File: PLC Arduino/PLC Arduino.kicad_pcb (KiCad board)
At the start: 2 copper layers, 145 x 75 mm, 208 parts, among them J1 Screw_Terminal_01x12, J2 Screw_Terminal_01x12, J3 Screw_Terminal_01x12, J4 Screw_Terminal_01x12, J5 USB_B_Micro, J6 Conn_01x04_Socket, J7 Conn_01x03_Socket, J8 Conn_01x02_Socket, J9 Conn_01x02_Socket, K1 SANYOU_SRD_Form_C, K2 SANYOU_SRD_Form_C, K3 SANYOU_SRD_Form_C, K5 SANYOU_SRD_Form_C, Q1 Q_NMOS_Depletion_GSD, Q10 BSS138, Q2 Q_NMOS_Depletion_GSD, Q3 Q_NMOS_Depletion_GSD, Q4 Q_NMOS_Depletion_GSD, Q5 Q_NMOS_Depletion_GSD, Q6 Q_NMOS_Depletion_GSD, Q7 Q_NMOS_Depletion_GSD, Q8 Q_NMOS_Depletion_GSD, Q9 BSS138, SW1 SW_Push, SW2 SW_Push, U1 PC817, U10 PC817, U11 PC817, U12 PC817, U13 PC817, U14 PC817, U15 PC817, U16 PC817, U18 ADS1115IDGS, U2 PC817, U22 ISO1540, U23 ESP32-WROOM-32, U24 CH340C, U25 MAX485E, U26 MAX485E, U27 TPL5010, U28 B0505S-2WR3, U29 LM2596S-5, U3 PC817, U30 AMS1117-3.3, U31 AMS1117-3.3, U32 74HC595, U33 74HC595, U34 74HC4051, U4 PC817, U5 PC817, U6 PC817, U7 PC817, U8 PC817, U9 PC817

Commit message: Done Layout PCB
To Do Zoning
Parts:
- removed C24: 220uF, Capacitor_SMD:C_Elec_6.3x7.7
- added C5: 100uF, Capacitor_SMD:C_1210_3225Metric_Pad1.33x2.70mm_HandSolder, F.Cu at (42.5, 26.6)
- added C6: 100uF, Capacitor_SMD:C_1210_3225Metric_Pad1.33x2.70mm_HandSolder, F.Cu at (46.0, 26.6)
- added J10: Conn_01x03_Socket, Connector_PinHeader_2.54mm:PinHeader_1x03_P2.54mm_Vertical, F.Cu at (145.3, 21.9)
- added J11: Conn_01x05_Socket, Connector_PinHeader_2.54mm:PinHeader_1x05_P2.54mm_Vertical, F.Cu at (145.3, 32.7)
- added J12: Conn_01x03_Socket, Connector_PinHeader_2.54mm:PinHeader_1x03_P2.54mm_Vertical, F.Cu at (136.5, 49.9)
- added J13: Conn_01x05_Socket, Connector_PinHeader_2.54mm:PinHeader_1x05_P2.54mm_Vertical, F.Cu at (63.9, 64.5)
- added J14: Screw_Terminal_01x08, TerminalBlock:TerminalBlock_bornier-8_P5.08mm, F.Cu at (183.8, 19.8)
- added J15: Screw_Terminal_01x08, TerminalBlock:TerminalBlock_bornier-8_P5.08mm, F.Cu at (127.8, 68.2)
- added JP19: SolderJumper_3_Open, Jumper:SolderJumper-3_P1.3mm_Open_Pad1.0x1.5mm, F.Cu at (59.3, 45.6)
- added REF**: MountingHole_3.2mm_M3, MountingHole:MountingHole_3.2mm_M3, F.Cu at (127.4, 29.5)
- added REF**: MountingHole_3.2mm_M3, MountingHole:MountingHole_3.2mm_M3, F.Cu at (181.8, 14.2)
- added REF**: MountingHole_3.2mm_M3, MountingHole:MountingHole_3.2mm_M3, F.Cu at (80.9, 29.5)
- added REF**: MountingHole_3.2mm_M3, MountingHole:MountingHole_3.2mm_M3, F.Cu at (86.7, 60.9)
- added REF**: MountingHole_3.2mm_M3, MountingHole:MountingHole_3.2mm_M3, F.Cu at (181.8, 60.7)
- added REF**: MountingHole_3.2mm_M3, MountingHole:MountingHole_3.2mm_M3, F.Cu at (150.4, 20.0)
- C23, C26: footprint Capacitor_SMD:C_Elec_10x10.2 -> Capacitor_SMD:C_1210_3225Metric_Pad1.33x2.70mm_HandSolder
- J4, JP11, JP12, JP13, JP14, JP15, JP16, JP17, JP18: moved to B.Cu
- moved R62 278.1 mm to (30.1, 61.7), turned to 0 degrees
- moved R64 276.7 mm to (30.1, 59.5), turned to 180 degrees
- moved R63 275.3 mm to (30.1, 57.4), turned to 0 degrees
- moved C32 268.5 mm to (63.5, 45.5), turned to 0 degrees
- moved R56 268.0 mm to (48.4, 61.9), turned to 0 degrees
- moved R77 268.0 mm to (61.7, 41.6), turned to -90 degrees
- moved R58 266.3 mm to (48.4, 59.7), turned to 180 degrees
- moved R76 265.7 mm to (63.1, 41.6), turned to -90 degrees
- moved C33 265.2 mm to (64.5, 43.8), turned to 180 degrees
- moved U26 264.6 mm to (36.5, 59.5), turned to 180 degrees
- moved R57 264.5 mm to (48.4, 57.5), turned to 0 degrees
- moved C17 262.3 mm to (52.0, 63.1)
- moved C16 261.9 mm to (53.0, 64.8), turned to 180 degrees
- moved C18 261.2 mm to (34.8, 64.9), turned to 180 degrees
- moved U22 255.8 mm to (67.9, 40.3), turned to 180 degrees
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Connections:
- C1 pad 1: +5VA -> 5VOUT
- C2 pad 2: +5VA -> 5VOUT
- C21 pad 2: +5VA -> 5VOUT
- C23 pad 1: DC_IN_1_B -> 5VOUT
- C23 pad 2: +5VA -> DC_IN_1_B
- C26 pad 1: GNDD -> +5V
- C26 pad 2: +5V -> GNDD
- C27 pad 1: +5VA -> 5VOUT
- C28 pad 2: +5VA -> 5VOUT
- C29 pad 2: +3.3VA -> 3.3VOUT
- C7 pad 2: +5VA -> 5VOUT
- C8 pad 1: +5VA -> 5VOUT
- D10 pad 2: +24V -> 24V_EXT
- D12 pad 2: +24V -> 24V_EXT
- D6 pad 2: +24V -> 24V_EXT
- D7 pad 2: +24V -> 24V_EXT
- J2 pad 5: SLAVE_MODBUS_A -> unconnected-(J2-Pin_5-Pad5)
- J2 pad 6: SLAVE_MODBUS_B -> unconnected-(J2-Pin_6-Pad6)
- J3 pad 1: DC_OUT_1_A -> _DC_OUT_1_A
- J3 pad 2: DC_OUT_1_B -> _DC_OUT_1_B
- J3 pad 3: DC_OUT_2_A -> _DC_OUT_2_A
- J3 pad 4: DC_OUT_2_B -> _DC_OUT_2_B
- J3 pad 5: DC_OUT_3_A -> _DC_OUT_3_A
- J3 pad 6: DC_OUT_3_B -> _DC_OUT_3_B
- J3 pad 7: DC_OUT_4_A -> _DC_OUT_4_A
- J3 pad 8: DC_OUT_4_B -> _DC_OUT_4_B
- J4 pad 10: 5VOUT -> unconnected-(J4-Pin_10-Pad10)
- J4 pad 2: unconnected-(J4-Pin_2-Pad2) -> SLAVE_MODBUS_A
- J4 pad 3: unconnected-(J4-Pin_3-Pad3) -> SLAVE_MODBUS_B
- J4 pad 5: unconnected-(J4-Pin_5-Pad5) -> DC_IN_1_B
- J4 pad 6: DC_IN_1_B -> SCL_E
- J4 pad 7: SCL_E -> SDA_E
- J4 pad 8: SDA_E -> unconnected-(J4-Pin_8-Pad8)
- J4 pad 9: 3.3VOUT -> unconnected-(J4-Pin_9-Pad9)
- J8 pad 2: +5VA -> 5VOUT
- JP10 pad 1: +5VA -> 5VOUT
- JP10 pad 3: +3.3VA -> 3.3VOUT
- JP2 pad 2: +5VA -> 5VOUT
- JP3 pad 1: +5VA -> 5VOUT
- JP3 pad 3: +3.3VA -> 3.3VOUT
- K1 pad 5: +24V -> 24V_EXT
- K2 pad 5: +24V -> 24V_EXT
- K3 pad 5: +24V -> 24V_EXT
- K5 pad 5: +24V -> 24V_EXT
- L1 pad 2: +5VA -> 5VOUT
- Q5 pad 2: DC_IN_1_B -> GND_ANALOG_EXT
- Q6 pad 2: DC_IN_1_B -> GND_ANALOG_EXT
- Q7 pad 2: DC_IN_1_B -> GND_ANALOG_EXT
- Q8 pad 2: DC_IN_1_B -> GND_ANALOG_EXT
- R13 pad 2: DC_IN_1_B -> GND_ANALOG_EXT
- R14 pad 1: DC_DRV_2 -> DC_DRV_2_EXT
- R15 pad 1: +24V -> 24V_EXT
- R16 pad 1: DC_DRV_1 -> DC_DRV_1_EXT
- R17 pad 1: +24V -> 24V_EXT
- R18 pad 2: DC_IN_1_B -> GND_ANALOG_EXT
- R19 pad 1: DC_DRV_3 -> DC_DRV_3_EXT
- R20 pad 1: +24V -> 24V_EXT
- R21 pad 2: DC_IN_1_B -> GND_ANALOG_EXT
- R22 pad 1: DC_DRV_4 -> DC_DRV_4_EXT
- R23 pad 1: +24V -> 24V_EXT
- R24 pad 2: DC_IN_1_B -> GND_ANALOG_EXT
- R67 pad 1: +5VA -> 5VOUT
- R78 pad 2: +5VA -> 5VOUT
- R79 pad 2: +5VA -> 5VOUT
- U18 pad 8: +5VA -> 5VOUT
- U22 pad 1: +5VA -> 5VOUT
- U23 pad 13: SLAVE_RO -> DIG_IN
- U23 pad 16: SLAVE_DI -> WDT_DONE
- U23 pad 30: WDT_DONE -> SLAVE_DI
- U23 pad 31: DIG_IN -> SLAVE_RO
- U28 pad 1: +5VA -> 5VOUT
- U30 pad 2: +3.3VA -> 3.3VOUT
- U30 pad 3: +5VA -> 5VOUT
- U5 pad 1: +3.3V -> 3v3_EXT
- U5 pad 4: VCOUPLER -> VCOUPLER_EXT
- U6 pad 1: +3.3V -> 3v3_EXT
- U6 pad 4: VCOUPLER -> VCOUPLER_EXT
- U7 pad 1: +3.3V -> 3v3_EXT
- U7 pad 4: VCOUPLER -> VCOUPLER_EXT
- U8 pad 1: +3.3V -> 3v3_EXT
- U8 pad 4: VCOUPLER -> VCOUPLER_EXT
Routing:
- net GNDD: track 0.00 -> 487.8 mm, vias 0 -> 33
- net DC_IN_1_B: track 0.00 -> 471.7 mm, vias 0 -> 117
- net +5V: track 0.00 -> 320.3 mm, vias 0 -> 13
- net +3.3V: track 0.00 -> 316.0 mm, vias 0 -> 18
- net +24V: track 0.00 -> 249.7 mm, vias 0 -> 8
- net 5VOUT: track 0.00 -> 232.4 mm, vias 0 -> 7
- net 24V_EXT: track 0.00 -> 139.8 mm, vias 0 -> 4
- net GND_ANALOG_EXT: track 0.00 -> 137.1 mm, vias 0 -> 6
- net DIG_IN: track 0.00 -> 115.3 mm, vias 0 -> 4
- net 3.3VOUT: track 0.00 -> 104.3 mm, vias 0 -> 1
- net VCOUPLER: track 0.00 -> 100.4 mm, vias 0 -> 6
- net SDA_E: track 0.00 -> 97.7 mm, vias 0 -> 4
- net SCL_E: track 0.00 -> 97.1 mm, vias 0 -> 4
- net 3v3_EXT: track 0.00 -> 93.7 mm
- net ESP_SCL: track 0.00 -> 86.4 mm, vias 0 -> 2
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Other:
- board size 145 x 75 mm -> 195.3 x 75 mm

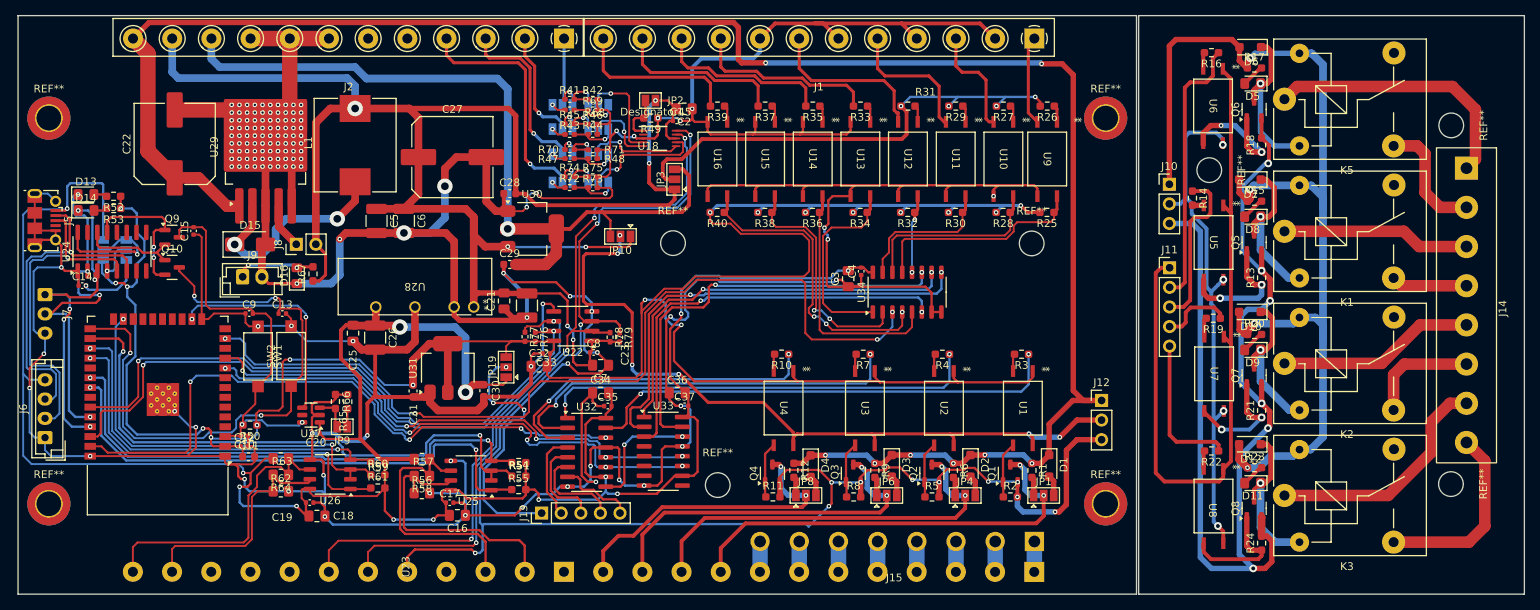
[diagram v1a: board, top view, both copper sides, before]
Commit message: Done PCB Layout PLC Board
To DO:

Review from Nes
Round Corners of Strobe and PLC
Proper Labels PLC Board
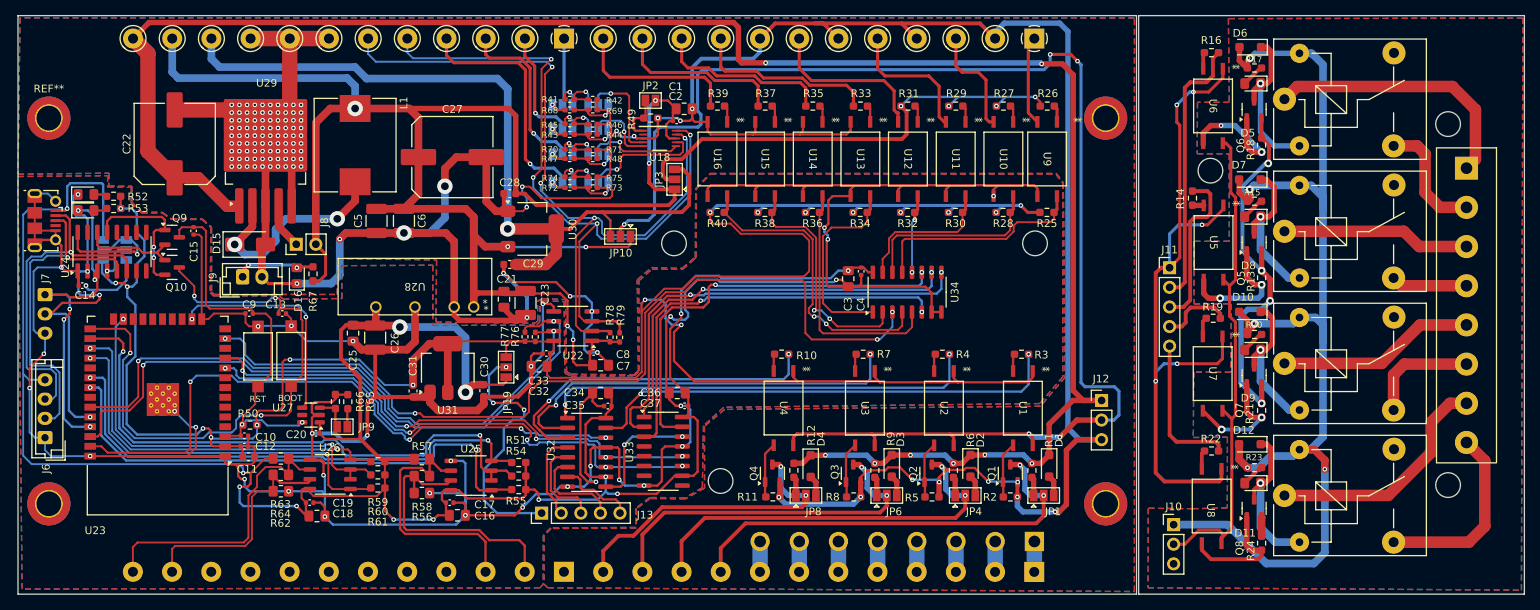
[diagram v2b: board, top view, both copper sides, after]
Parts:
- removed the REF** at (127.4, 29.5)
- removed the REF** at (181.8, 14.2)
- removed the REF** at (80.9, 29.5)
- removed the REF** at (86.7, 60.9)
- removed the REF** at (181.8, 60.7)
- removed the REF** at (150.4, 20.0)
- added REF**: MountingHole_3.2mm_M3, MountingHole:MountingHole_3.2mm_M3, F.Cu at (181.4, 60.9)
- added REF**: MountingHole_3.2mm_M3, MountingHole:MountingHole_3.2mm_M3, F.Cu at (87.1, 60.3)
- added REF**: MountingHole_3.2mm_M3, MountingHole:MountingHole_3.2mm_M3, F.Cu at (150.6, 20.1)
- added REF**: MountingHole_3.2mm_M3, MountingHole:MountingHole_3.2mm_M3, F.Cu at (81.0, 29.5)
- added REF**: MountingHole_3.2mm_M3, MountingHole:MountingHole_3.2mm_M3, F.Cu at (127.8, 29.5)
- added REF**: MountingHole_3.2mm_M3, MountingHole:MountingHole_3.2mm_M3, F.Cu at (181.4, 14.1)
- moved J10 44.1 mm to (145.8, 66.0)
- moved C23 0.38 mm to (61.8, 37.2)
- moved U8 0.24 mm to (150.7, 63.6)
- moved C21 0.22 mm to (59.0, 36.8)
- moved U7 0.19 mm to (150.9, 46.4)
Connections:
- J2 pad 5: unconnected-(J2-Pin_5-Pad5) -> SCL_E
- J2 pad 6: unconnected-(J2-Pin_6-Pad6) -> SDA_E
- J4 pad 5: DC_IN_1_B -> unconnected-(J4-Pin_5-Pad5)
- J4 pad 6: SCL_E -> unconnected-(J4-Pin_6-Pad6)
- J4 pad 7: SDA_E -> unconnected-(J4-Pin_7-Pad7)
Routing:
- net GND_ANALOG_EXT: track 137.1 -> 51.7 mm, vias 6 -> 4
- net VCOUPLER: track 100.4 -> 181.4 mm, vias 6 -> 5
- net DC_IN_1_B: track 471.7 -> 443.9 mm, vias 117 -> 114
- net 24V_EXT: track 139.8 -> 149.9 mm, vias 4 -> 5
- net VCOUPLER_EXT: track 67.5 -> 64.2 mm, vias 4 -> 0
- net SCL_E: track 97.1 -> 94.3 mm
- net 3v3_EXT: track 93.7 -> 95.4 mm, vias 0 -> 5
- net SDA_E: track 97.7 -> 96.0 mm
- net DIN_4: vias 3 -> 2
- added copper zone on B.Cu, net DC_IN_1_B
- added copper zone on F.Cu, net DC_IN_1_B
- added copper zone on B.Cu, net GNDD
- added copper zone on F.Cu, net GNDD
- added copper zone on B.Cu, net GND_ANALOG_EXT
- added copper zone on F.Cu, net GND_ANALOG_EXT
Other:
- board text added: "BOOT"
- board text added: "RST"

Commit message: Version 1.0 of both Strobe Light and PLC Done
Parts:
- added G***: LOGO, InnovationCentral:logo_8mm, B.Cu at (122.2, 46.9)
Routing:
- net GND_ANALOG_EXT: vias 4 -> 98
- net GNDD: vias 33 -> 60
- net DC_IN_1_B: vias 114 -> 143
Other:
- board size 195.3 x 75 mm -> 195.2 x 75 mm
- board text added: "1"
- board text added: "2"
- board text added: "24V"
- board text added: "3"
- board text added: "3.3V"
- board text added: "3V3"
- board text added: "4"
- board text added: "5V"
- board text added: "A"
- board text added: "A1"
- board text added: "A2"
- board text added: "A3"
- board text added: "A4"
- board text added: "B"
- board text added: "BY: ENGR. CHARLES KIM KABILING 08-25-24"
- board text added: "BYP"
- board text added: "D+"
- board text added: "D-"
- board text added: "DC1"
- board text added: "DC2"
- board text added: "DC3"
- board text added: "DC4"
- board text added: "DCI-1"
- board text added: "DCI-2"
- board text added: "DCI-3"
- board text added: "DCI-4"
- board text added: "DESIGNED AND MANUFACTURED BY:"
- board text added: "DRIVING INNOVATION FOR LONG TERM SOLUTIONS"
- board text added: "ESP32-PLC V1.0"
- board text added: "G"
- board text added: "I1"
- board text added: "I2"
- board text added: "I3"
- board text added: "I4"
- board text added: "INNOVATION CENTRAL PH"
- board text added: "MASTER"
- board text added: "O1"
- board text added: "O2"
- board text added: "O3"
- board text added: "O4"
- board text added: "R"
- board text added: "SCL"
- board text added: "SDA"
- board text added: "T"
- board text added: "V"
- board text added: "VCC"
